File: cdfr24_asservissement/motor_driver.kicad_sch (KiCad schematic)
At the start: 13 parts

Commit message: Finish routing
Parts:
- renumbered R16 to R15
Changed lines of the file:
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@@
 		(dnp no)
 		(fields_autoplaced yes)
-		(property "Reference" "R16"
+		(property "Reference" "R15"
 			(at 197.104 102.87 0)
 			(effects
@@
 			(project "cdfr24_asservissement"
 				(path "/c6b82269-16f5-49e6-8b51-4d12a40a3077/084e419c-7880-44c5-a0d2-721d5e789f19"
-					(reference "R16")
+					(reference "R15")
 					(unit 1)
 				)

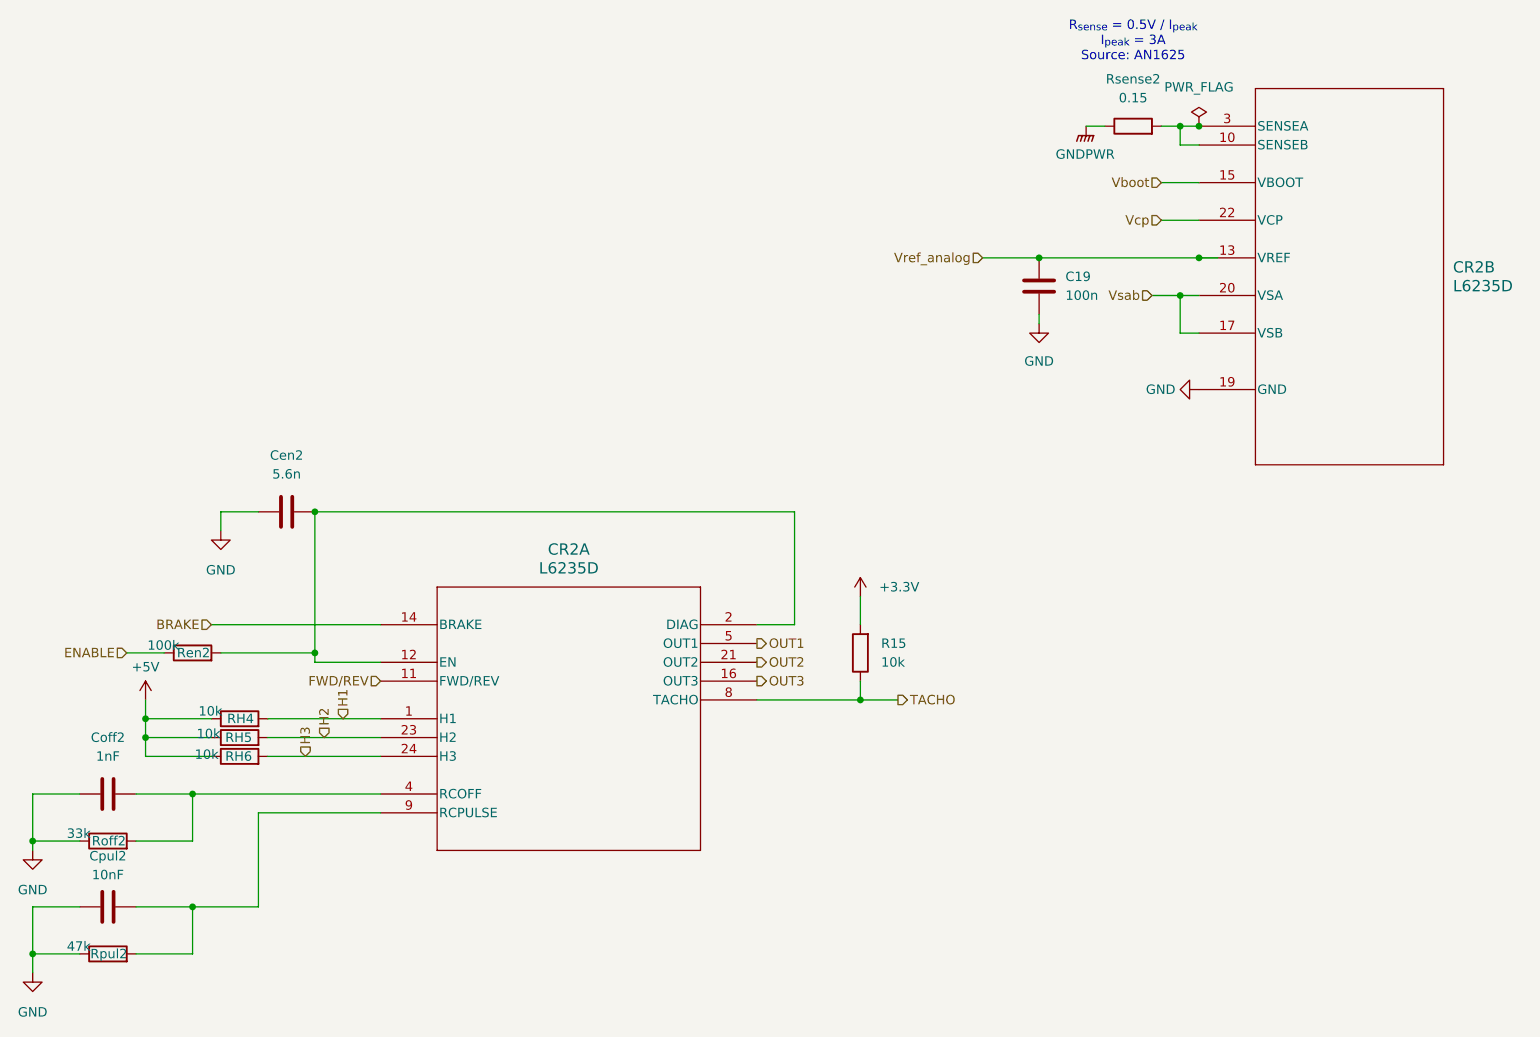
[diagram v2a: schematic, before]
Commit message: Add silkscreen and logo
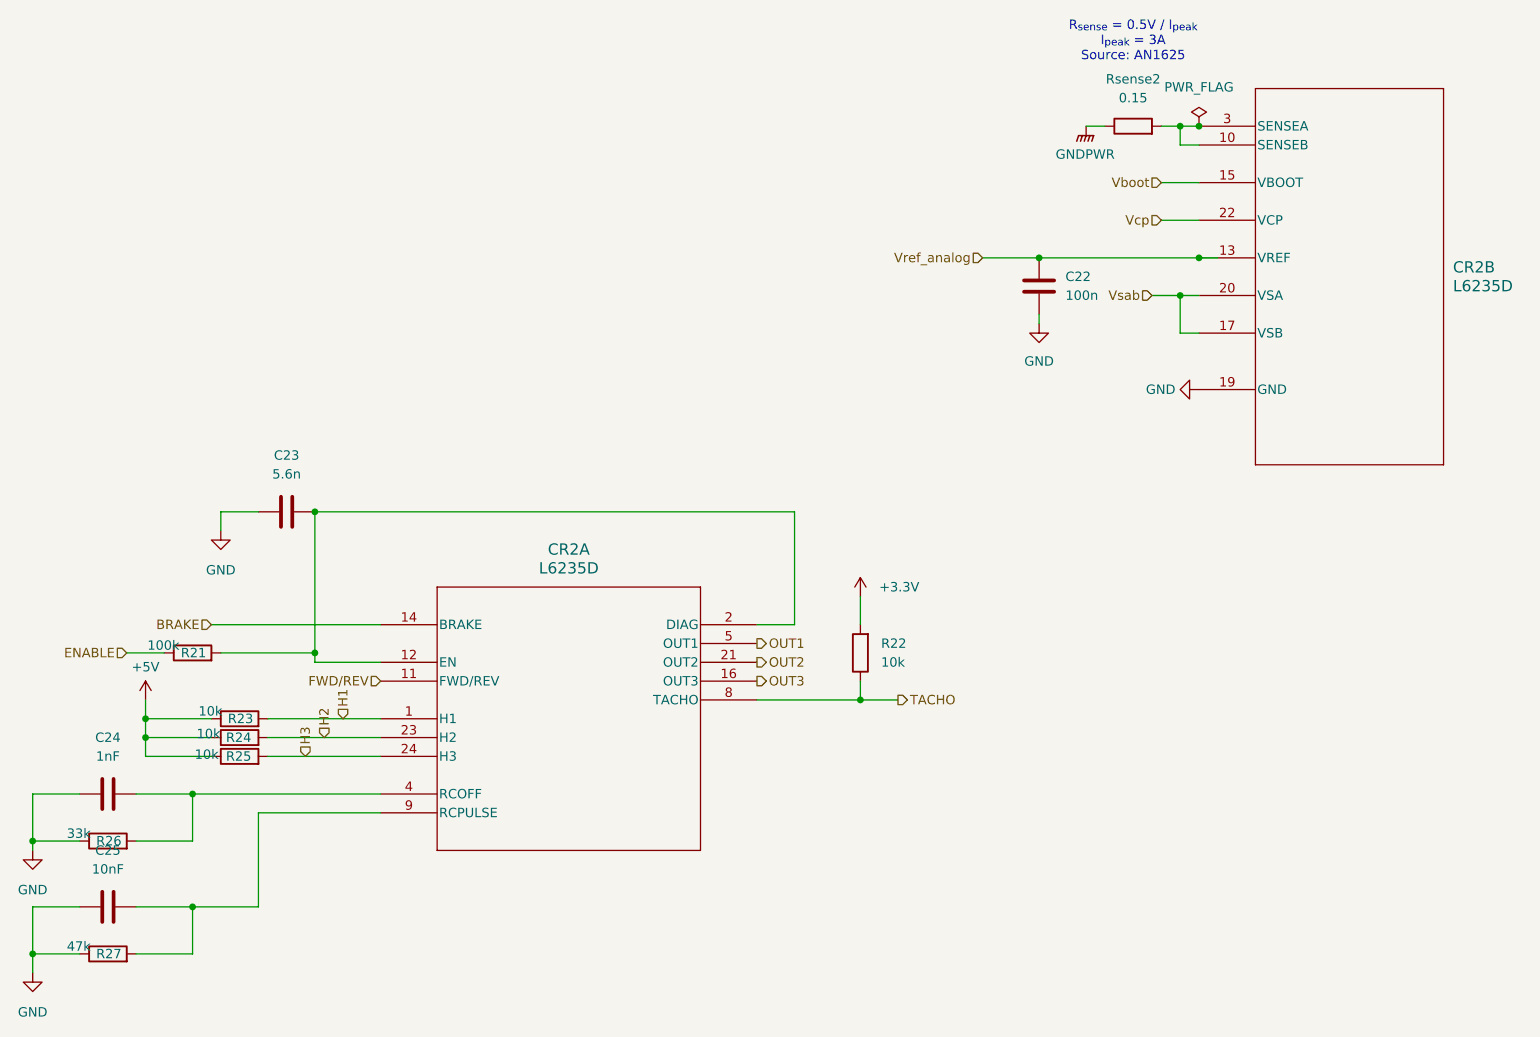
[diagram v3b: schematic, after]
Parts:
- renumbered C19 to C22, Cen2 to C23, Coff2 to C24, Cpul2 to C25, Ren2 to R21, R15 to R22, RH4 to R23, RH5 to R24, RH6 to R25, Roff2 to R26, Rpul2 to R27
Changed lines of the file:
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@@
 		(on_board yes)
 		(dnp no)
-		(property "Reference" "RH6"
+		(property "Reference" "R25"
 			(at 110.363 118.11 90)
 			(effects
@@
 			(project "cdfr24_asservissement"
 				(path "/c6b82269-16f5-49e6-8b51-4d12a40a3077/084e419c-7880-44c5-a0d2-721d5e789f19"
-					(reference "RH6")
-					(unit 1)
-				)
-				(path "/c6b82269-16f5-49e6-8b51-4d12a40a3077/fbaa2c7d-8eee-479f-b1be-bb54414743c2"
-					(reference "RH3")
+					(reference "R25")
+					(unit 1)
+				)
+				(path "/c6b82269-16f5-49e6-8b51-4d12a40a3077/fbaa2c7d-8eee-479f-b1be-bb54414743c2"
+					(reference "R18")
 					(unit 1)
 				)
@@
 		(dnp no)
 		(fields_autoplaced yes)
-		(property "Reference" "Cpul2"
-			(at 92.71 131.572 90)
+		(property "Reference" "C25"
+			(at 92.71 130.81 90)
 			(effects
 				(font
@@
 		)
 		(property "Value" "10nF"
-			(at 92.71 134.112 90)
+			(at 92.71 133.35 90)
 			(effects
 				(font
@@
 			(project "cdfr24_asservissement"
 				(path "/c6b82269-16f5-49e6-8b51-4d12a40a3077/084e419c-7880-44c5-a0d2-721d5e789f19"
-					(reference "Cpul2")
-					(unit 1)
-				)
-				(path "/c6b82269-16f5-49e6-8b51-4d12a40a3077/fbaa2c7d-8eee-479f-b1be-bb54414743c2"
-					(reference "Cpul1")
+					(reference "C25")
+					(unit 1)
+				)
+				(path "/c6b82269-16f5-49e6-8b51-4d12a40a3077/fbaa2c7d-8eee-479f-b1be-bb54414743c2"
+					(reference "C21")
 					(unit 1)
 				)
@@
 		(on_board yes)
 		(dnp no)
-		(property "Reference" "RH4"
+		(property "Reference" "R23"
 			(at 110.617 113.03 90)
 			(effects
@@
 			(project "cdfr24_asservissement"
 				(path "/c6b82269-16f5-49e6-8b51-4d12a40a3077/084e419c-7880-44c5-a0d2-721d5e789f19"
-					(reference "RH4")
-					(unit 1)
-				)
-				(path "/c6b82269-16f5-49e6-8b51-4d12a40a3077/fbaa2c7d-8eee-479f-b1be-bb54414743c2"
-					(reference "RH1")
+					(reference "R23")
+					(unit 1)
+				)
+				(path "/c6b82269-16f5-49e6-8b51-4d12a40a3077/fbaa2c7d-8eee-479f-b1be-bb54414743c2"
+					(reference "R16")
 					(unit 1)
 				)
@@
 		(on_board yes)
 		(dnp no)
-		(property "Reference" "Roff2"
+		(property "Reference" "R26"
 			(at 92.837 129.54 90)
 			(effects
@@
 			(project "cdfr24_asservissement"
 				(path "/c6b82269-16f5-49e6-8b51-4d12a40a3077/084e419c-7880-44c5-a0d2-721d5e789f19"
-					(reference "Roff2")
-					(unit 1)
-				)
-				(path "/c6b82269-16f5-49e6-8b51-4d12a40a3077/fbaa2c7d-8eee-479f-b1be-bb54414743c2"
-					(reference "Roff1")
+					(reference "R26")
+					(unit 1)
+				)
+				(path "/c6b82269-16f5-49e6-8b51-4d12a40a3077/fbaa2c7d-8eee-479f-b1be-bb54414743c2"
+					(reference "R19")
 					(unit 1)
 				)
@@
 		(dnp no)
 		(fields_autoplaced yes)
-		(property "Reference" "Coff2"
+		(property "Reference" "C24"
 			(at 92.71 115.57 90)
 			(effects
@@
 			(project "cdfr24_asservissement"
 				(path "/c6b82269-16f5-49e6-8b51-4d12a40a3077/084e419c-7880-44c5-a0d2-721d5e789f19"
-					(reference "Coff2")
-					(unit 1)
-				)
-				(path "/c6b82269-16f5-49e6-8b51-4d12a40a3077/fbaa2c7d-8eee-479f-b1be-bb54414743c2"
-					(reference "Coff1")
+					(reference "C24")
+					(unit 1)
+				)
+				(path "/c6b82269-16f5-49e6-8b51-4d12a40a3077/fbaa2c7d-8eee-479f-b1be-bb54414743c2"
+					(reference "C20")
 					(unit 1)
 				)
@@
 		(on_board yes)
 		(dnp no)
-		(property "Reference" "Ren2"
+		(property "Reference" "R21"
 			(at 104.267 104.14 90)
 			(effects
@@
 			(project "cdfr24_asservissement"
 				(path "/c6b82269-16f5-49e6-8b51-4d12a40a3077/084e419c-7880-44c5-a0d2-721d5e789f19"
-					(reference "Ren2")
-					(unit 1)
-				)
-				(path "/c6b82269-16f5-49e6-8b51-4d12a40a3077/fbaa2c7d-8eee-479f-b1be-bb54414743c2"
-					(reference "Ren1")
+					(reference "R21")
+					(unit 1)
+				)
+				(path "/c6b82269-16f5-49e6-8b51-4d12a40a3077/fbaa2c7d-8eee-479f-b1be-bb54414743c2"
+					(reference "R14")
 					(unit 1)
 				)
@@
 		(on_board yes)
 		(dnp no)
-		(property "Reference" "Rpul2"
+		(property "Reference" "R27"
 			(at 92.837 144.78 90)
 			(effects
@@
 			(project "cdfr24_asservissement"
 				(path "/c6b82269-16f5-49e6-8b51-4d12a40a3077/084e419c-7880-44c5-a0d2-721d5e789f19"
-					(reference "Rpul2")
-					(unit 1)
-				)
-				(path "/c6b82269-16f5-49e6-8b51-4d12a40a3077/fbaa2c7d-8eee-479f-b1be-bb54414743c2"
-					(reference "Rpul1")
+					(reference "R27")
+					(unit 1)
+				)
+				(path "/c6b82269-16f5-49e6-8b51-4d12a40a3077/fbaa2c7d-8eee-479f-b1be-bb54414743c2"
+					(reference "R20")
 					(unit 1)
 				)
@@
 		(dnp no)
 		(fields_autoplaced yes)
-		(property "Reference" "R15"
+		(property "Reference" "R22"
 			(at 197.104 102.87 0)
 			(effects
@@
 			(project "cdfr24_asservissement"
 				(path "/c6b82269-16f5-49e6-8b51-4d12a40a3077/084e419c-7880-44c5-a0d2-721d5e789f19"
+					(reference "R22")
+					(unit 1)
+				)
+				(path "/c6b82269-16f5-49e6-8b51-4d12a40a3077/fbaa2c7d-8eee-479f-b1be-bb54414743c2"
 					(reference "R15")
-					(unit 1)
-				)
-				(path "/c6b82269-16f5-49e6-8b51-4d12a40a3077/fbaa2c7d-8eee-479f-b1be-bb54414743c2"
-					(reference "R14")
 					(unit 1)
 				)
@@
 		(dnp no)
 		(fields_autoplaced yes)
-		(property "Reference" "Cen2"
+		(property "Reference" "C23"
 			(at 116.84 77.47 90)
 			(effects
@@
 			(project "cdfr24_asservissement"
 				(path "/c6b82269-16f5-49e6-8b51-4d12a40a3077/084e419c-7880-44c5-a0d2-721d5e789f19"
-					(reference "Cen2")
-					(unit 1)
-				)
-				(path "/c6b82269-16f5-49e6-8b51-4d12a40a3077/fbaa2c7d-8eee-479f-b1be-bb54414743c2"
-					(reference "Cen1")
+					(reference "C23")
+					(unit 1)
+				)
+				(path "/c6b82269-16f5-49e6-8b51-4d12a40a3077/fbaa2c7d-8eee-479f-b1be-bb54414743c2"
+					(reference "C19")
 					(unit 1)
 				)
@@
 		(dnp no)
 		(fields_autoplaced yes)
-		(property "Reference" "C19"
+		(property "Reference" "C22"
 			(at 221.996 53.34 0)
 			(effects
@@
 			(project "cdfr24_asservissement"
 				(path "/c6b82269-16f5-49e6-8b51-4d12a40a3077/084e419c-7880-44c5-a0d2-721d5e789f19"
-					(reference "C19")
+					(reference "C22")
 					(unit 1)
 				)
@@
 		(on_board yes)
 		(dnp no)
-		(property "Reference" "RH5"
+		(property "Reference" "R24"
 			(at 110.363 115.57 90)
 			(effects
@@
 			(project "cdfr24_asservissement"
 				(path "/c6b82269-16f5-49e6-8b51-4d12a40a3077/084e419c-7880-44c5-a0d2-721d5e789f19"
-					(reference "RH5")
-					(unit 1)
-				)
-				(path "/c6b82269-16f5-49e6-8b51-4d12a40a3077/fbaa2c7d-8eee-479f-b1be-bb54414743c2"
-					(reference "RH2")
-					(unit 1)
-				)
+					(reference "R24")
+					(unit 1)
+				)
+				(path "/c6b82269-16f5-49e6-8b51-4d12a40a3077/fbaa2c7d-8eee-479f-b1be-bb54414743c2"
+					(reference "R17")
+					(unit 1)
+				)
